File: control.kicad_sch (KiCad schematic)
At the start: 18 parts, among them U16001 OPA2810

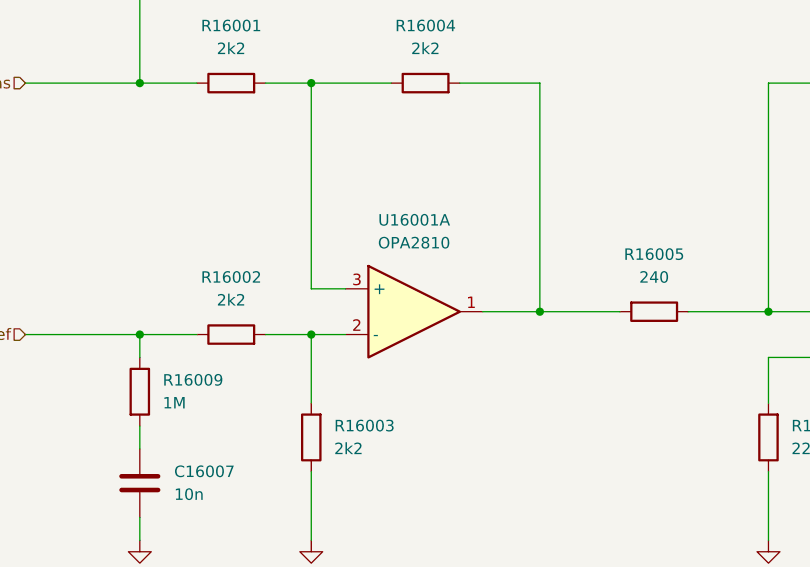
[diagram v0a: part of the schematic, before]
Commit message: fix control difference junction switched inputs
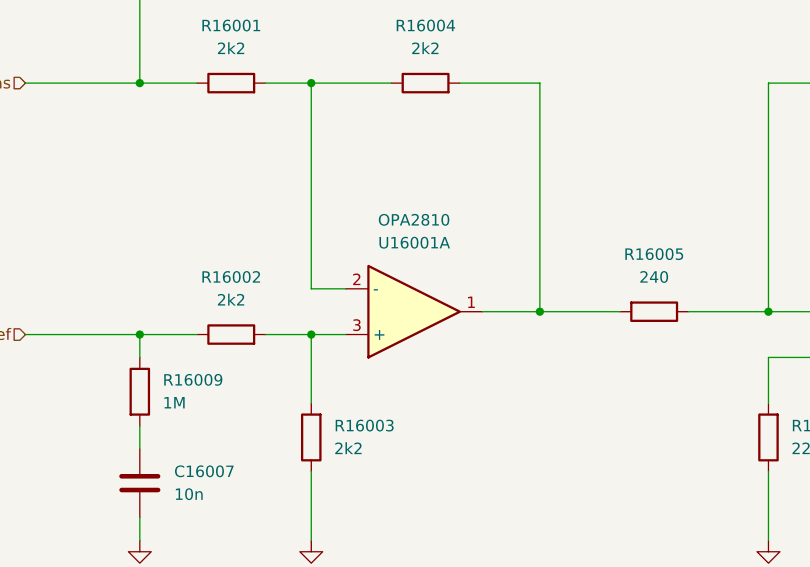
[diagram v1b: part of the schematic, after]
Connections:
- net at R16001.2, R16004.1: now also U16001.2 (-); no longer U16001.3 (+)
- net at R16002.2, R16003.2: now also U16001.3 (+); no longer U16001.2 (-)
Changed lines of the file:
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@@
 		(lib_id "pss:Opamp_Dual")
 		(at 132.08 101.6 0)
+		(mirror x)
 		(unit 1)
 		(exclude_from_sim no)
@@
 		(on_board yes)
 		(dnp no)
-		(fields_autoplaced yes)
 		(property "Reference" "U16001"
-			(at 132.08 91.44 0)
+			(at 132.08 93.98 0)
 			(effects
 				(font
@@
 		)
 		(property "Value" "OPA2810"
-			(at 132.08 93.98 0)
+			(at 132.08 91.44 0)
 			(effects
 				(font

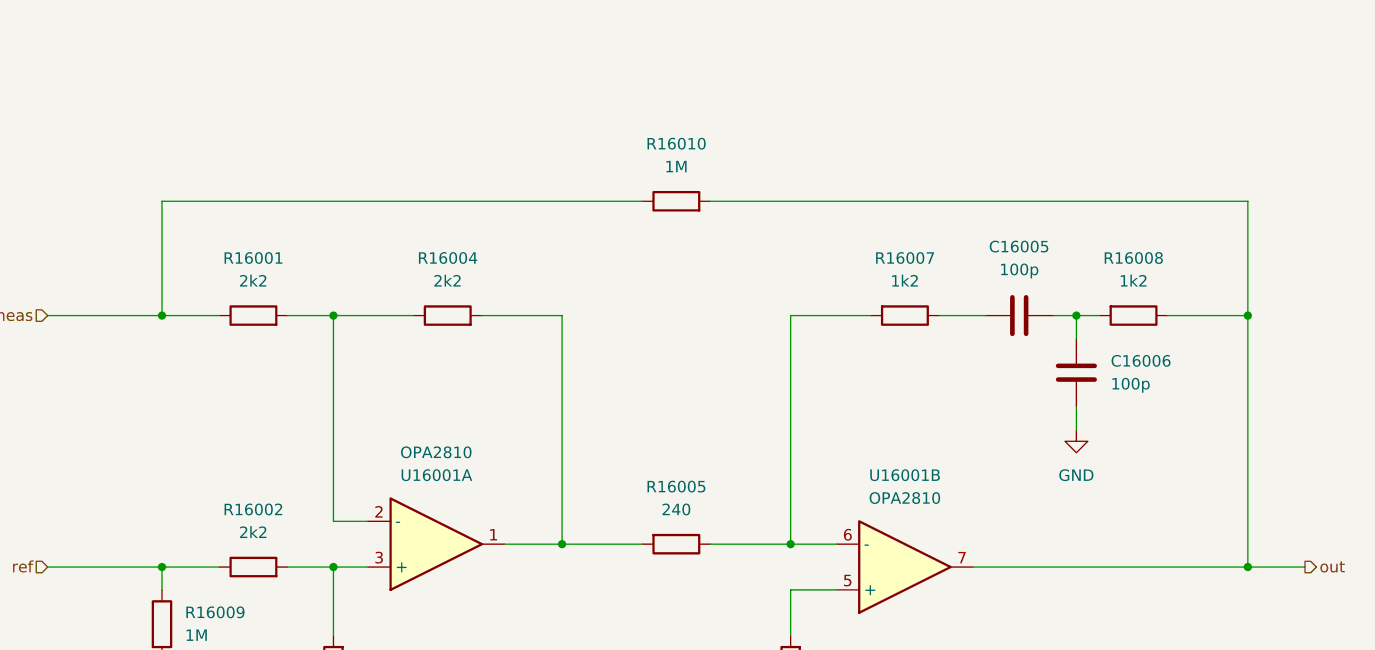
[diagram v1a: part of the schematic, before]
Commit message: fix control pid controller circuit
circuit in Europalehrbuch Tabellenbuch Elektrotechnik which is listed under 'pid controller' is not a pid controller.
circuit is redesigned as described in docs by designing the pid with RC networks.
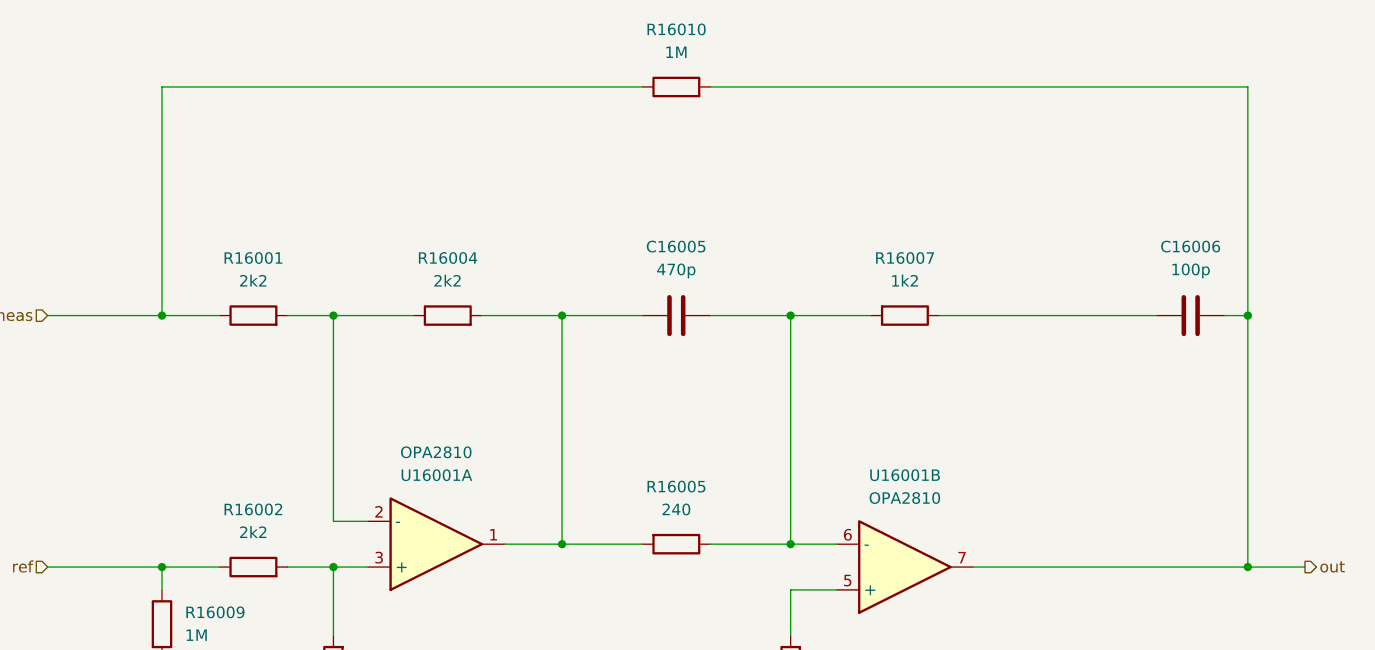
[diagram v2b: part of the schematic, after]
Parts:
- removed R16008: 1k2, Resistor_SMD:R_1210_3225Metric_Pad1.30x2.65mm_HandSolder, symbol pss:R
- C16005: value 100p -> 470p; MPN C0805C101J5GACTU -> C0805C471J5GACTU; VPN 80-C0805C101J5G -> 80-C0805C471J5G
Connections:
- net GND: no longer C16006.2
- net out: now also C16006.2
- net at R16004.2, R16005.2, U16001.1: now also C16005.1
- net at R16007.1: now also C16006.1; no longer C16005.1
- net at C16005.2: now also R16005.1, R16007.2, U16001.6 (-); no longer C16006.1
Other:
- moved on the sheet: C16005, C16006, R16010

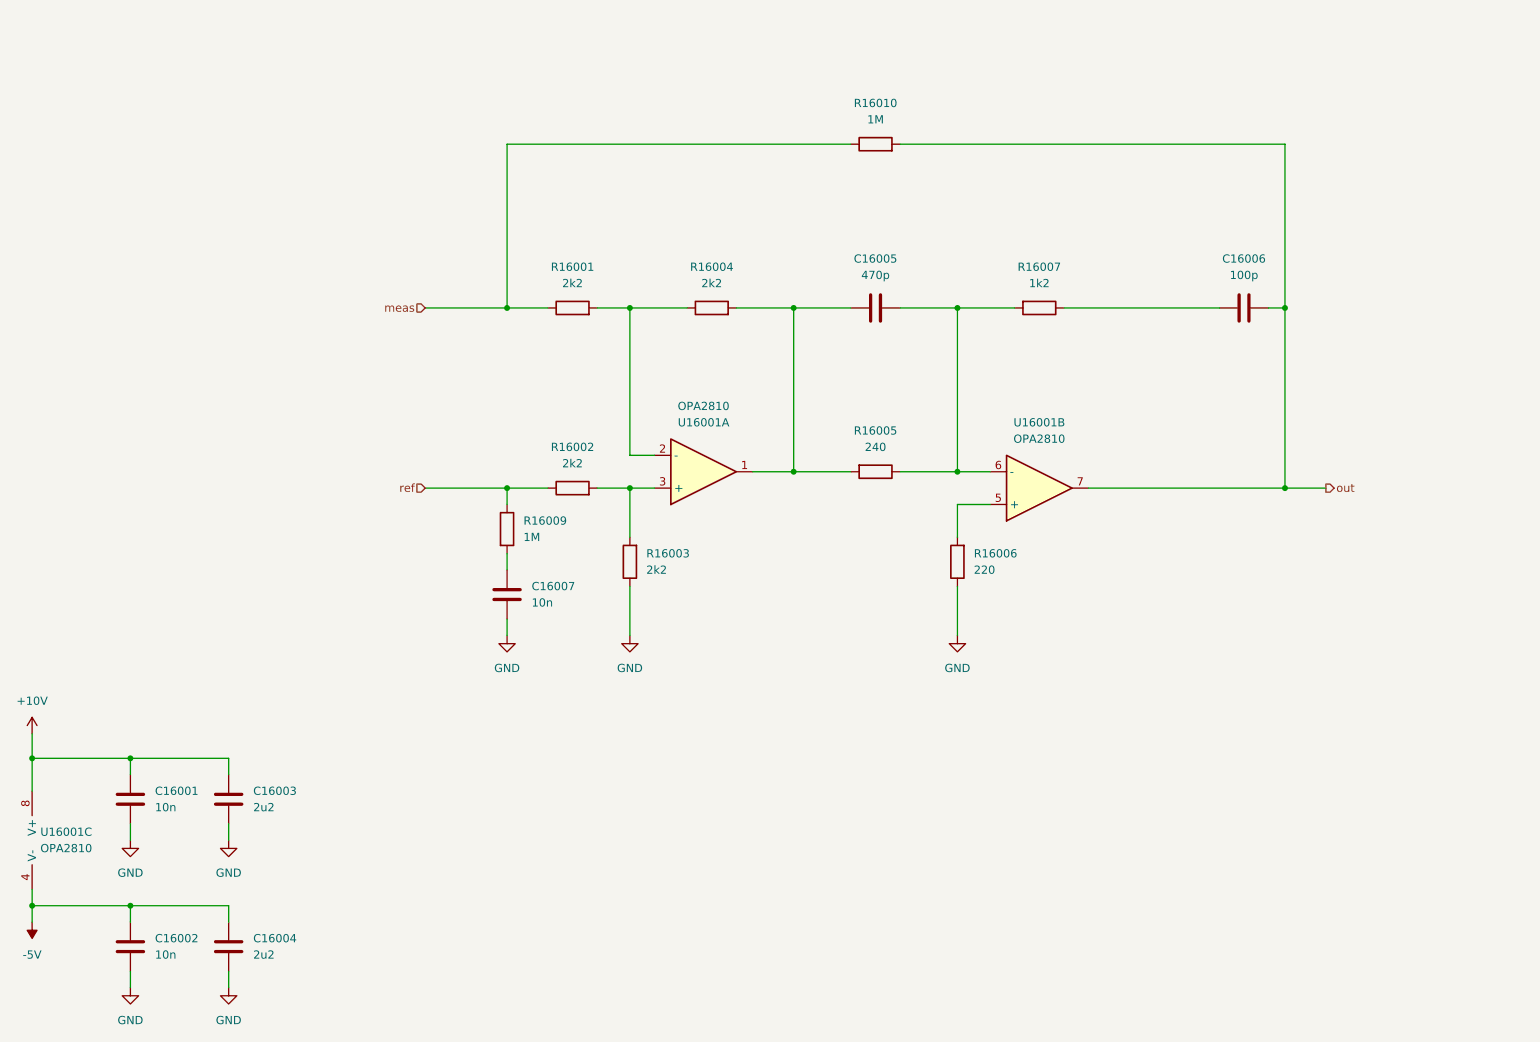
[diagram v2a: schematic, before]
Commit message: add control pid anit integral windup diodes
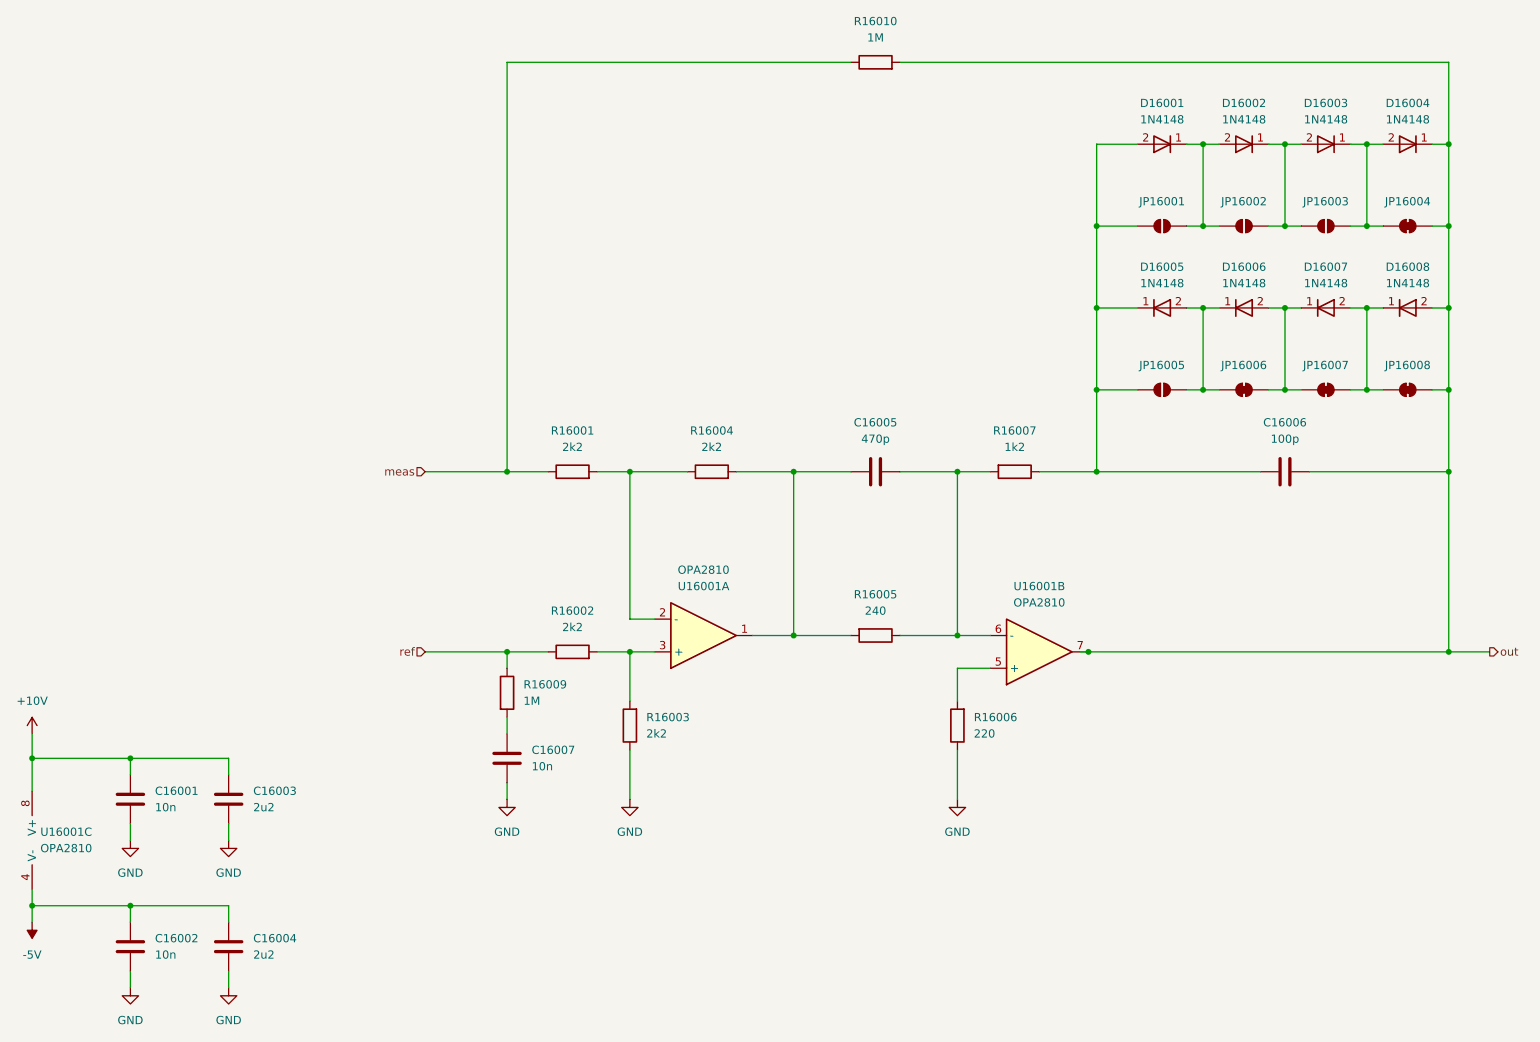
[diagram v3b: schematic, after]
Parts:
- added D16001, D16002, D16003, D16004, D16005, D16006, D16007, D16008: 1N4148, Diode_SMD:D_SOD-123, symbol Device:D
- added JP16001, JP16002, JP16003, JP16005: SolderJumper_2_Open, symbol Jumper:SolderJumper_2_Open
- added JP16004, JP16006, JP16007, JP16008: SolderJumper_2_Bridged, symbol Jumper:SolderJumper_2_Bridged
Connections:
- net out: now also D16004.1 (K), D16008.2 (A), JP16004.2 (B), JP16008.2 (B)
- net at C16006.1, R16007.1: now also D16001.2 (A), D16005.1 (K), JP16001.1 (A), JP16005.1 (A)
- new net: D16002.1 (K), D16003.2 (A), JP16002.2 (B), JP16003.1 (A)
- new net: D16001.1 (K), D16002.2 (A), JP16001.2 (B), JP16002.1 (A)
- new net: D16007.2 (A), D16008.1 (K), JP16007.2 (B), JP16008.1 (A)
- new net: D16003.1 (K), D16004.2 (A), JP16003.2 (B), JP16004.1 (A)
- new net: D16006.2 (A), D16007.1 (K), JP16006.2 (B), JP16007.1 (A)
- new net: D16005.2 (A), D16006.1 (K), JP16005.2 (B), JP16006.1 (A)
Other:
- moved on the sheet: C16005, C16006, C16007, R16001, R16002, R16003, R16004, R16005, R16006, R16007, R16009, R16010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
